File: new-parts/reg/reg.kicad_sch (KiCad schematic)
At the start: 51 parts, among them J1 BHR-10-VUA, J2 BHR-10-VUA, J3 BHR-10-VUA, J4 BHR-10-VUA, J5 Conn_01x02, J6 Conn_02x02_Odd_Even, K1 J104D2C12VDC.15S, K10 J104D2C12VDC.15S, K11 J104D2C12VDC.15S, K12 J104D2C12VDC.15S, K2 J104D2C12VDC.15S, K3 J104D2C12VDC.15S, K4 J104D2C12VDC.15S, K5 J104D2C12VDC.15S, K6 J104D2C12VDC.15S, K7 J104D2C12VDC.15S, K8 J104D2C12VDC.15S, K9 J104D2C12VDC.15S

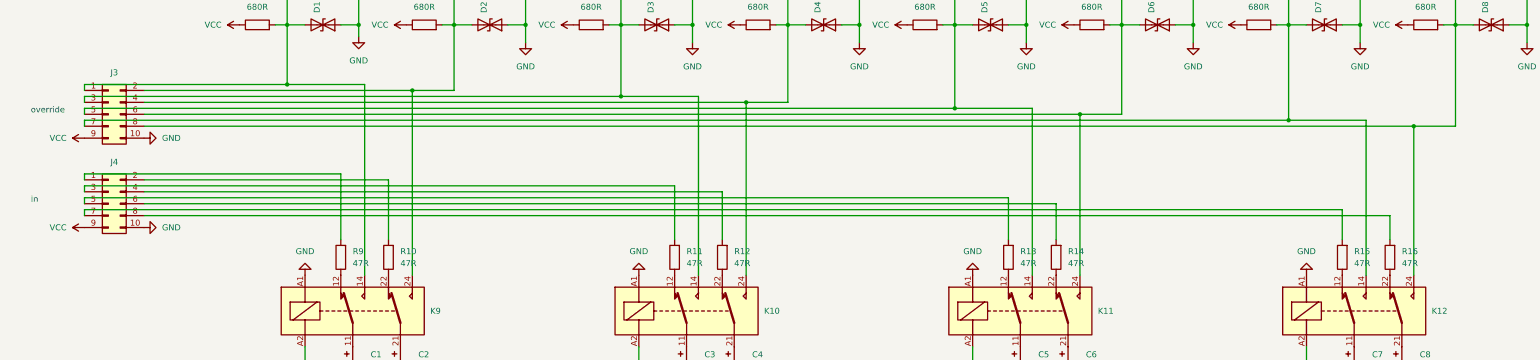
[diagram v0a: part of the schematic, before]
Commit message: Reverse clock polarity.
It's more convenient to have the registers sample the input while the
clock is high, and latch it to the output on the falling edge. That way,
a register whose clock input is kept low or Z will not change (otherwise,
we would have to keep idle registers' clock inputs high).
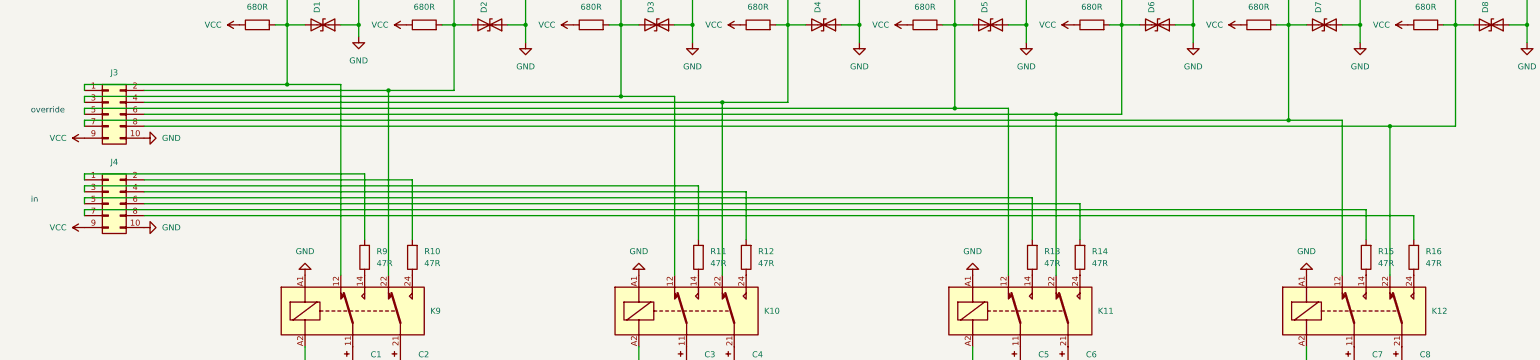
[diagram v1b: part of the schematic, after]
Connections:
- net at D2.2 (A2), J3.2 (Pin_2), K2.A1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: now also K9.22; no longer K9.24
- net at R12.1: now also K10.24; no longer K10.22
- net at K9.12: now also D1.2 (A2), J3.1 (Pin_1), K1.A1, R1.2; no longer R9.1
- net at R10.1: now also K9.24; no longer K9.22
- net at D4.2 (A2), J3.4 (Pin_4), K4.A1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: now also K10.22; no longer K10.24
- net at D5.2 (A2), J3.5 (Pin_5), K5.A1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: now also K11.12; no longer K11.14
- net at R16.1: now also K12.24; no longer K12.22
- net at R13.1: now also K11.14; no longer K11.12
- net at K12.12: now also D7.2 (A2), J3.7 (Pin_7), K7.A1, R7.2; no longer R15.1
- net at D8.2 (A2), J3.8 (Pin_8), K8.A1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: now also K12.22; no longer K12.24
- net at R14.1: now also K11.24; no longer K11.22
- net at D6.2 (A2), J3.6 (Pin_6), K6.A1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: now also K11.22; no longer K11.24
- net at R11.1: now also K10.14; no longer K10.12
- net at D3.2 (A2), J3.3 (Pin_3), K3.A1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: now also K10.12; no longer K10.14
- new net: K9.14, R9.1
- new net: K12.14, R15.1
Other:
- moved on the sheet: R10, R11, R12, R13, R14, R15, R16, R9

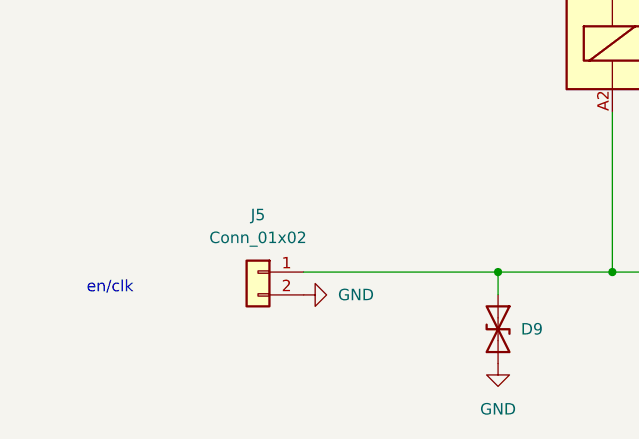
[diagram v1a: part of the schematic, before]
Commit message: Change all two-pin headers for control + ground to control only.
This is to prevent accidental short circuits when they are plugged in the
wrong way.
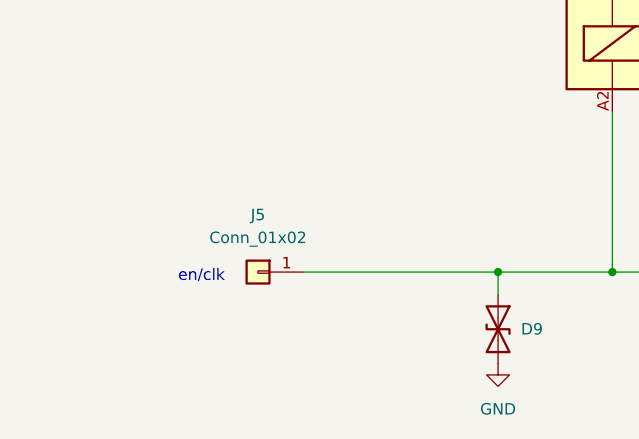
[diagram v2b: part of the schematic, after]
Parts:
- J5: footprint Connector_PinHeader_2.54mm:PinHeader_1x02_P2.54mm_Vertical -> Connector_PinHeader_2.54mm:PinHeader_1x01_P2.54mm_Vertical; symbol Connector_Generic:Conn_01x02 -> Connector_Generic:Conn_01x01
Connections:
- net GND: no longer J5.2 (Pin_2)
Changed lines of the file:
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@@
     (effects (font (size 1.27 1.27)) (justify left bottom))
   )
-  (text "en/clk" (at 24.13 195.58 0)
+  (text "en/clk" (at 34.29 194.31 0)
     (effects (font (size 1.27 1.27)) (justify left bottom))
   )
@@
     )
   )
-  (symbol (lib_id "Connector_Generic:Conn_01x02") (at 43.18 193.04 0) (mirror y) (unit 1)
+  (symbol (lib_id "Connector_Generic:Conn_01x01") (at 43.18 193.04 0) (mirror y) (unit 1)
     (in_bom yes) (on_board yes) (dnp no) (fields_autoplaced)
     (property "Reference" "J5" (at 43.18 186.69 0)
@@
       (effects (font (size 1.27 1.27)))
     )
-    (property "Footprint" "Connector_PinHeader_2.54mm:PinHeader_1x02_P2.54mm_Vertical" (at 43.18 193.04 0)
+    (property "Footprint" "Connector_PinHeader_2.54mm:PinHeader_1x01_P2.54mm_Vertical" (at 43.18 193.04 0)
       (effects (font (size 1.27 1.27)) hide)
     )
@@
       (effects (font (size 1.27 1.27)) hide)
     )
-    (pin "2")
     (pin "1")
     (instances
@@
         )
       )
-    )
-  )
-  (symbol (lib_id "power:GND") (at 48.26 195.58 90) (unit 1)
-    (in_bom yes) (on_board yes) (dnp no) (fields_autoplaced)
-    (property "Reference" "#PWR065" (at 54.61 195.58 0)
-      (effects (font (size 1.27 1.27)) hide)
-    )
-    (property "Value" "GND" (at 52.07 195.58 90)
-      (effects (font (size 1.27 1.27)) (justify right))
-    )
-    (property "Footprint" "" (at 48.26 195.58 0)
-      (effects (font (size 1.27 1.27)) hide)
-    )
-    (property "Datasheet" "" (at 48.26 195.58 0)
-      (effects (font (size 1.27 1.27)) hide)
-    )
-    (pin "1")
-    (instances
-      (project "reg"
-        (path "/8e7358e7-c3ef-4f3e-9154-e7eba01c544e"
-          (reference "#PWR065") (unit 1)
-        )
-      )

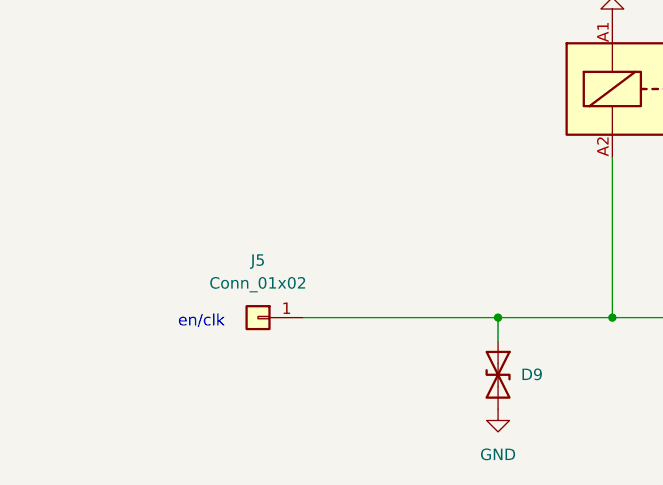
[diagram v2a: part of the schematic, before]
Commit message: Fix connector values: change names from 2 rows to 1 row.
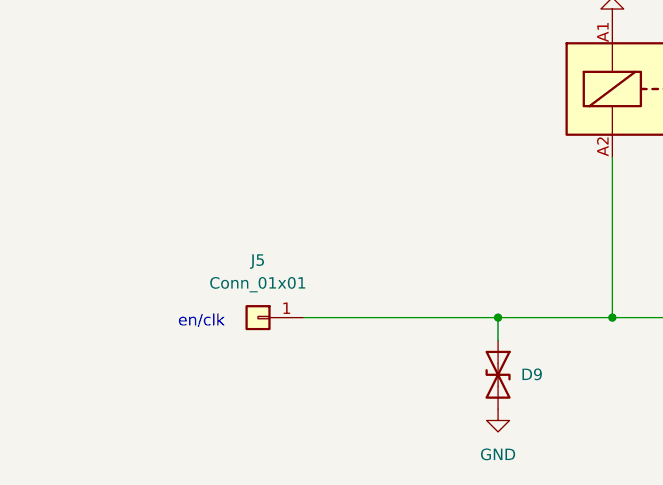
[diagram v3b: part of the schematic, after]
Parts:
- J5: value Conn_01x02 -> Conn_01x01
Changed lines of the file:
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@@
       (effects (font (size 1.27 1.27)))
     )
-    (property "Value" "Conn_01x02" (at 43.18 189.23 0)
+    (property "Value" "Conn_01x01" (at 43.18 189.23 0)
       (effects (font (size 1.27 1.27)))
     )
